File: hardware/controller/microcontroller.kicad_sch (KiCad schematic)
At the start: 37 parts, among them J1 USB_C_Receptacle_USB2.0_14P, J2 IDC-10, SW1 SW_Push, U1 USBLC6-2SC6, U2 STM32H523RETx, U3 ESP32-C3-WROOM-02, Y1 8MHz

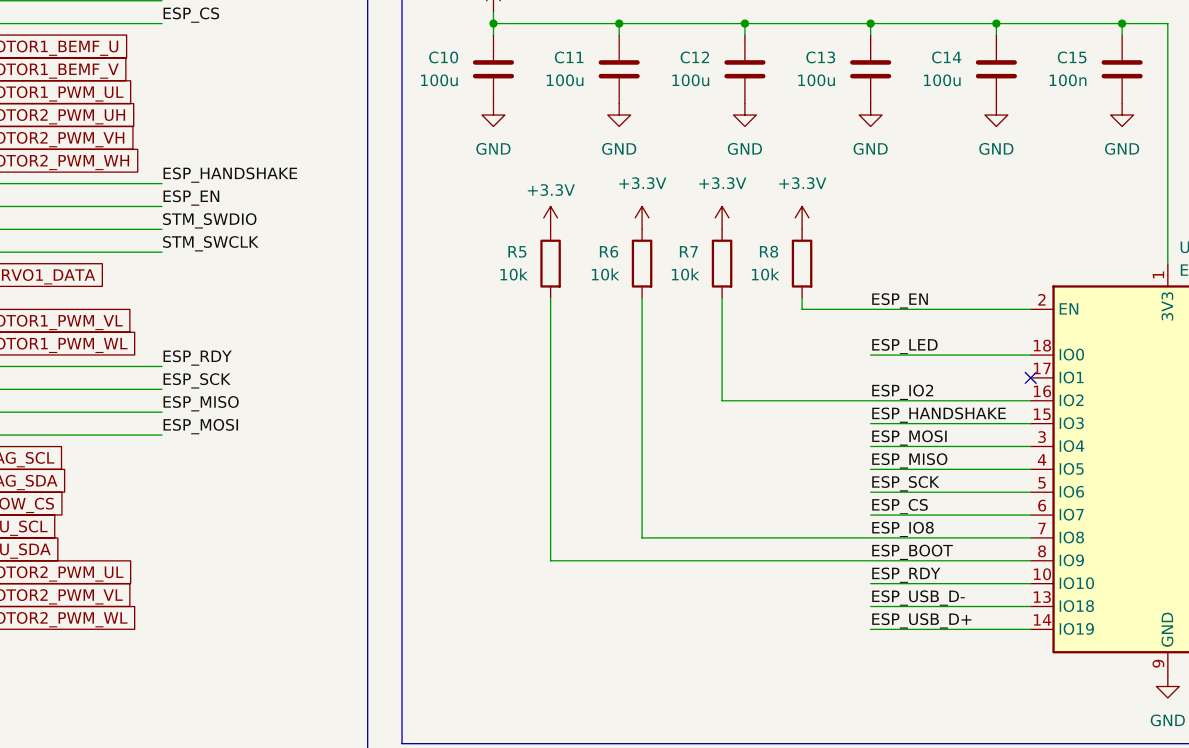
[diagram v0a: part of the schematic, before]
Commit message: rename signals to correct
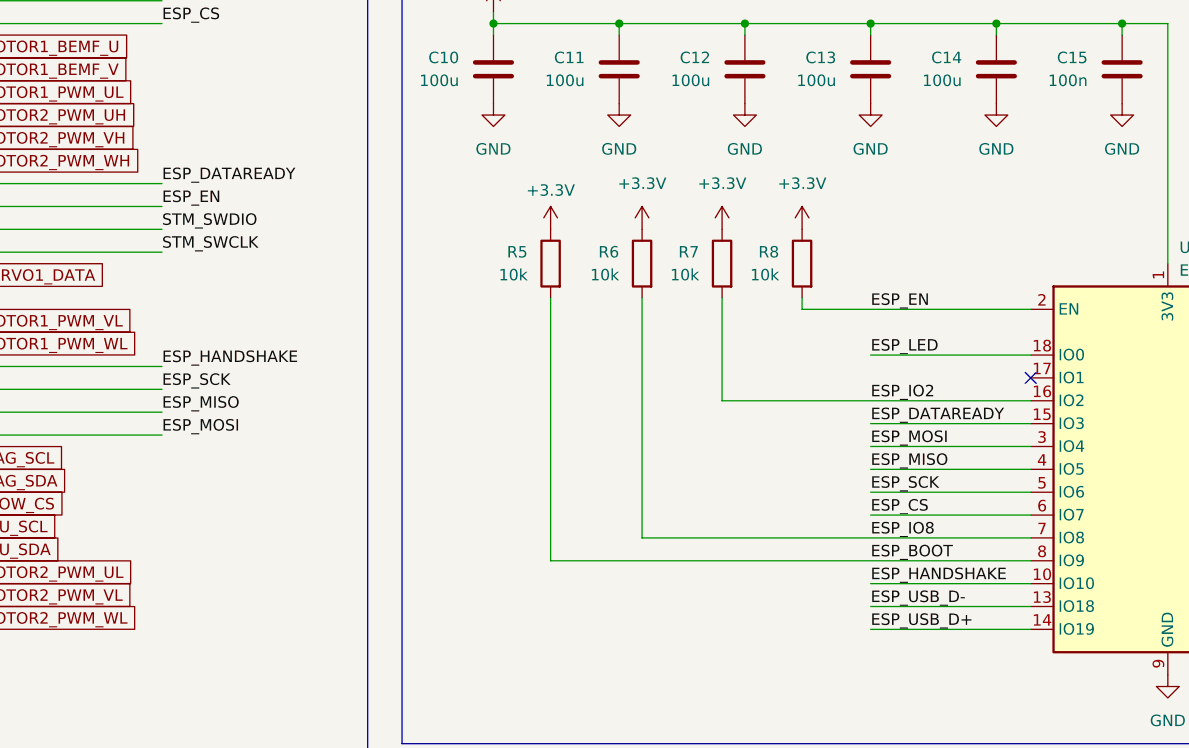
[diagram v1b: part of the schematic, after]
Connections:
- net ESP_RDY is gone; now on net ESP_HANDSHAKE: U2.28 (PB2), U3.10 (IO10)
- net ESP_HANDSHAKE: no longer U2.44 (PA11), U3.15 (IO3)
- new net ESP_DATAREADY: U2.44 (PA11), U3.15 (IO3)
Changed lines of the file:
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@@
 	(title_block
 		(title "Hogger2 Controller")
-		(date "2025-03-09")
+		(date "2025-04-12")
 		(rev "V1.1")
 		(comment 4 "Author: Eryk Możdżeń")
